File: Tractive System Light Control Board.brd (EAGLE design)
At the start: 88.2 x 39 mm, 70 parts, among them J1 MOLEX_CLICKMATE-2-VERTICAL, J2 MOLEX_CLICKMATE-2-VERTICAL, Q1 BSS138, T1 750313734, U1 ISO7221, U12 SN6501DBVR, U2 TPS562219, U21 LM1085IS, U3 SN74LVC1G04DRL, U36 LTC1155, U37 CSD17506Q5A, U38 LM124, U6 LTC1155, U8 CSD17506Q5A, U9 SN74LVC1G86DRL

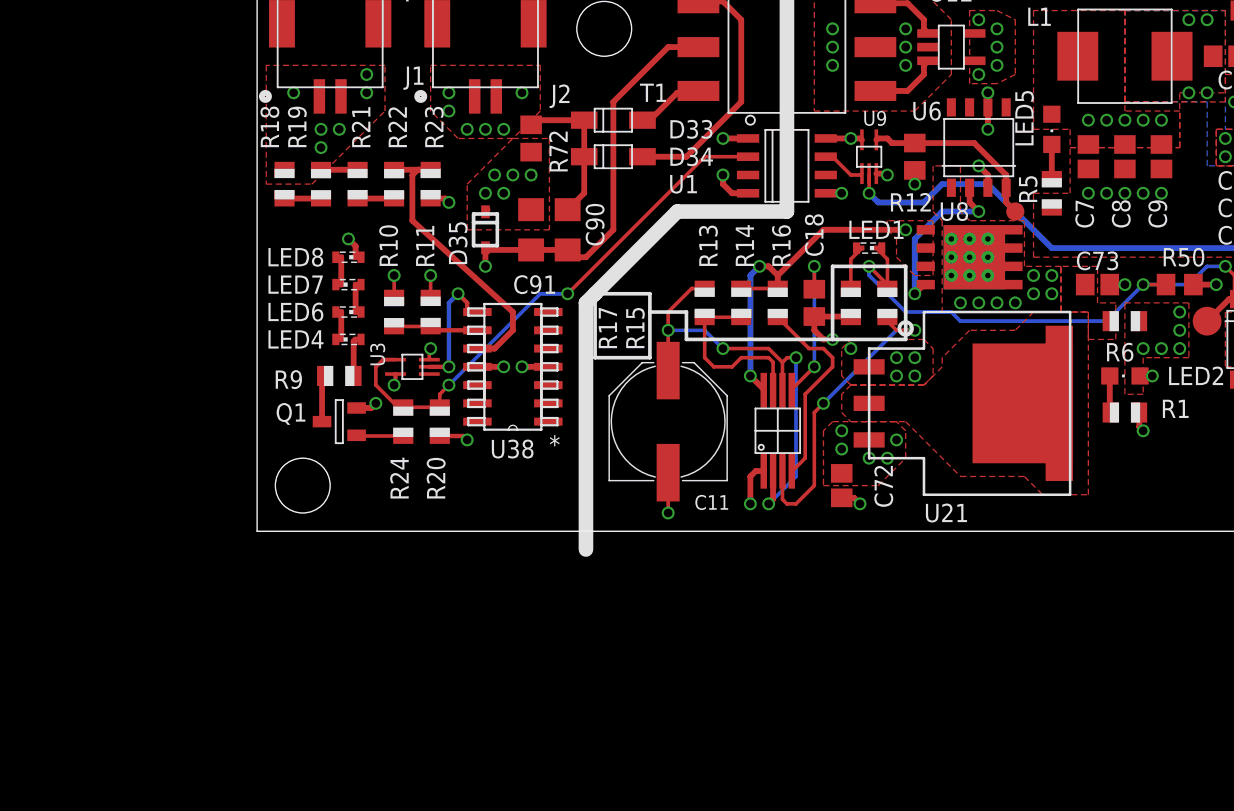
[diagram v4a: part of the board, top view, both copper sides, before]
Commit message: Reconfigured the schematic to improve functionality and readability
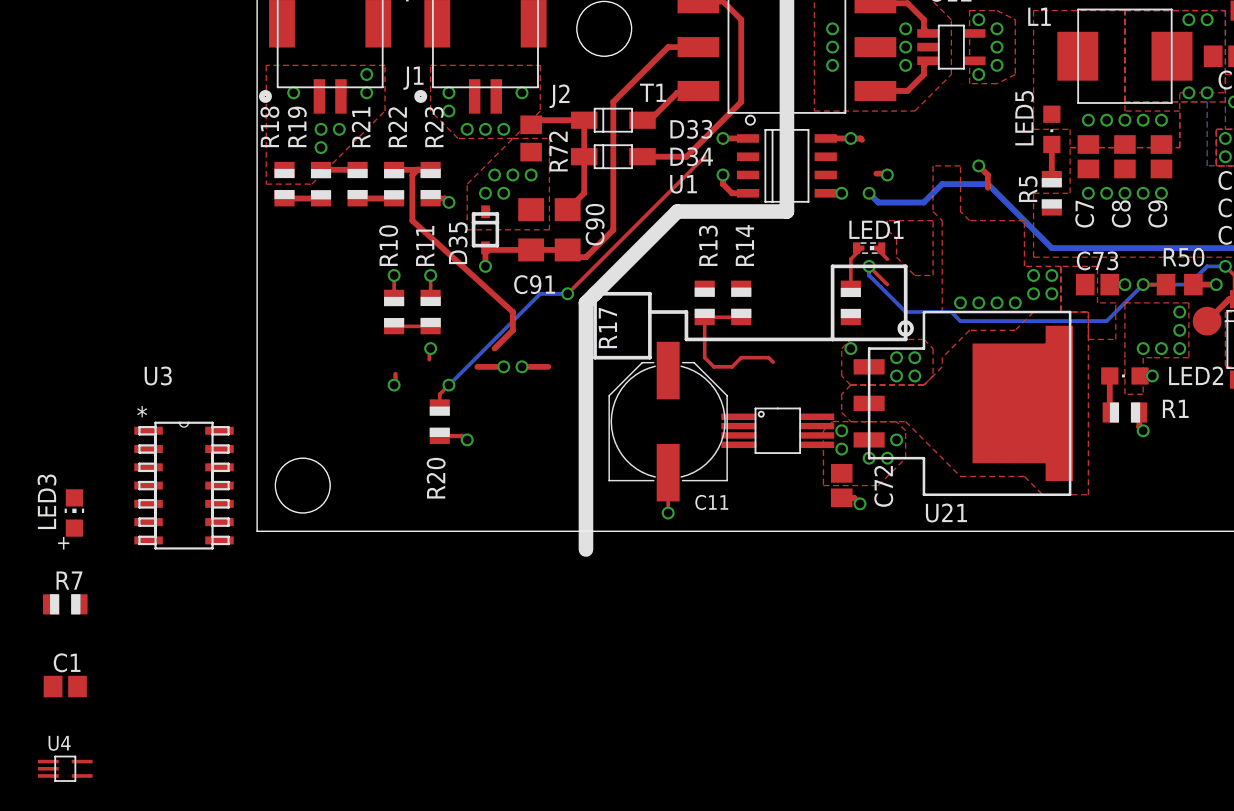
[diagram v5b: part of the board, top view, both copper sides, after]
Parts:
- removed C18: 100uF, rcl:C0805
- removed LED4, LED6, LED7, LED8: (no value), FormE:SMARTLED-TTW
- removed Q1: BSS138, FormE:BSS138
- removed R12: 10k, rcl:R0805
- removed R15: 0.33k, adafruit:R0805
- removed R16, R9: 1K, adafruit:R0805
- removed R24: 10, adafruit:R0805
- removed R6: 0.007, adafruit:R0805
- removed TP1: PTR1B1,27, testpad:B1,27
- removed U38: LM124, FormE:D14
- removed U6: LTC1155, FormE:LT-SOL8
- removed U8: CSD17506Q5A, FormE:SON_5X6
- removed U9: SN74LVC1G86DRL, FormE:LITTLE_LOGIC_BASIC_DRL
- added C1: 0.1uF, adafruit:C0805
- added LED3: (no value), FormE:CHIP-LED0805
- added R7: 10k, adafruit:R0805
- added U4: SN74LVC1G00DRL, FormE:LITTLE_LOGIC_BASIC_DRL
- J1, J2: value MOLEX_CLICKMATE-2-VERTICAL -> WM9811CT-ND
- R10: value 1.2k -> 10k
- R11: value 10k -> 47k
- R18: value 10k -> 140k
- R19, R21, R22: value 10k -> 120k
- T2: value (none) -> LMC555
- U3: value SN74LVC1G04DRL -> LM139; device FormE:LITTLE_LOGIC_BASIC_DRL -> FormE:D14
- moved U3 17.9 mm to (-5.08, 3.17), turned to 0 degrees
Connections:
- net LED_CONTROL_12V renamed TSAL_SUPPLY
- removed net 12V_CURRENT_SENSE+: C73.1, R6.1, U21.2, U21.GND, U21.GND1
- removed net 555_TIMER_SUPPLY: R14.1, R16.2, T2.P$1, U8.1, U8.2, U8.3
- removed net AMS_CONTACTOR_INVERTED: H1.4, U9.2
- removed net HV_INDICATOR_SIGNAL_LV: U1.P$7, U9.1
- removed net N$19: R16.1, T2.P$8
- removed net N$20: R15.1, T2.P$7
- removed net N$21: LED4.C@1, R9.2
- removed net N$22: LED4.A@1, LED6.C@1
- removed net N$24: LED6.A@1, LED7.C@1
- removed net N$25: LED7.A@1, LED8.C@1
- removed net N$35: U3.2, U38.8
- removed net N$49: Q1.G, R24.1
- removed net N$6: C11.+, R13.1, T2.P$3, T2.P$6
- removed net N$60: Q1.D, R9.1
- removed net N$8: U6.2, U8.4
- new net AIR_CLOSED: H1.4, U4.2
- new net N$4: U1.P$6, U4.1
- new net N$7: LED3.A, R7.2
- net +12V: now also C73.1, U21.2, U21.GND, U21.GND1; no longer R6.2
- net +5V: now also C1.1, R14.1, T2.8, U4.5; no longer U6.1, U6.6, U8.5, U8.6, U8.7, U8.8, U8.PAD, U8.PAD1, U8.VIA1, U8.VIA2, U8.VIA3, U8.VIA4, U8.VIA5, U8.VIA6, U8.VIA7, U8.VIA8, U8.VIA9, U9.5
- net +5V/1: now also R7.1, U3.3; no longer LED8.A@1, U3.5, U38.4
- net 555_TIMER_OUTPUT: now also T2.3; no longer R15.2
- net BATT_V_REFERENCE: now also U3.7; no longer U38.10
- net GND: now also C1.2, T2.1, U4.3; no longer C18.1, R12.1, T2.P$5, U6.3, U9.3
- net GND1: now also U3.12; no longer Q1.S, U3.3, U38.11
- net HV_INDICATOR_SIGNAL_HV: now also LED3.C, U1.P$3, U3.1; no longer R24.2, U1.P$2, U3.4
- net N$15: now also C11.+, R13.1, T2.2, T2.6; no longer C18.2, T2.P$4
- net N$48: now also U3.6; no longer U38.9
- net N$5: now also T2.7; no longer T2.P$2
- net N$9: now also T2.4, U4.4; no longer R12.2, TP1.TP, U6.4, U9.4
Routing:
- net AMS_CONTACTOR_INVERTED: track 47.4 -> 0.00 mm, vias 2 -> 0
- net AIR_CLOSED: track 0.00 -> 46.0 mm, vias 0 -> 2
- net N$6: track 32.5 -> 0.00 mm, vias 4 -> 0
- net 555_TIMER_SUPPLY: track 24.5 -> 0.00 mm, vias 3 -> 0
- net N$20: track 21.7 -> 0.00 mm, vias 2 -> 0
- net N$19: track 14.0 -> 0.00 mm
- net N$9: track 12.9 -> 0.00 mm
- net N$8: track 12.2 -> 0.00 mm, vias 2 -> 0
- net HV_INDICATOR_SIGNAL_HV: track 37.1 -> 26.2 mm
- net N$15: track 10.9 -> 0.00 mm, vias 2 -> 0
- net GND: track 28.7 -> 19.3 mm, vias 41 -> 38
- net N$35: track 8.95 -> 0.00 mm, vias 2 -> 0
- net N$60: track 3.64 -> 0.00 mm
- net N$49: track 3.27 -> 0.00 mm
- net HV_INDICATOR_SIGNAL_LV: track 3.08 -> 0.00 mm
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
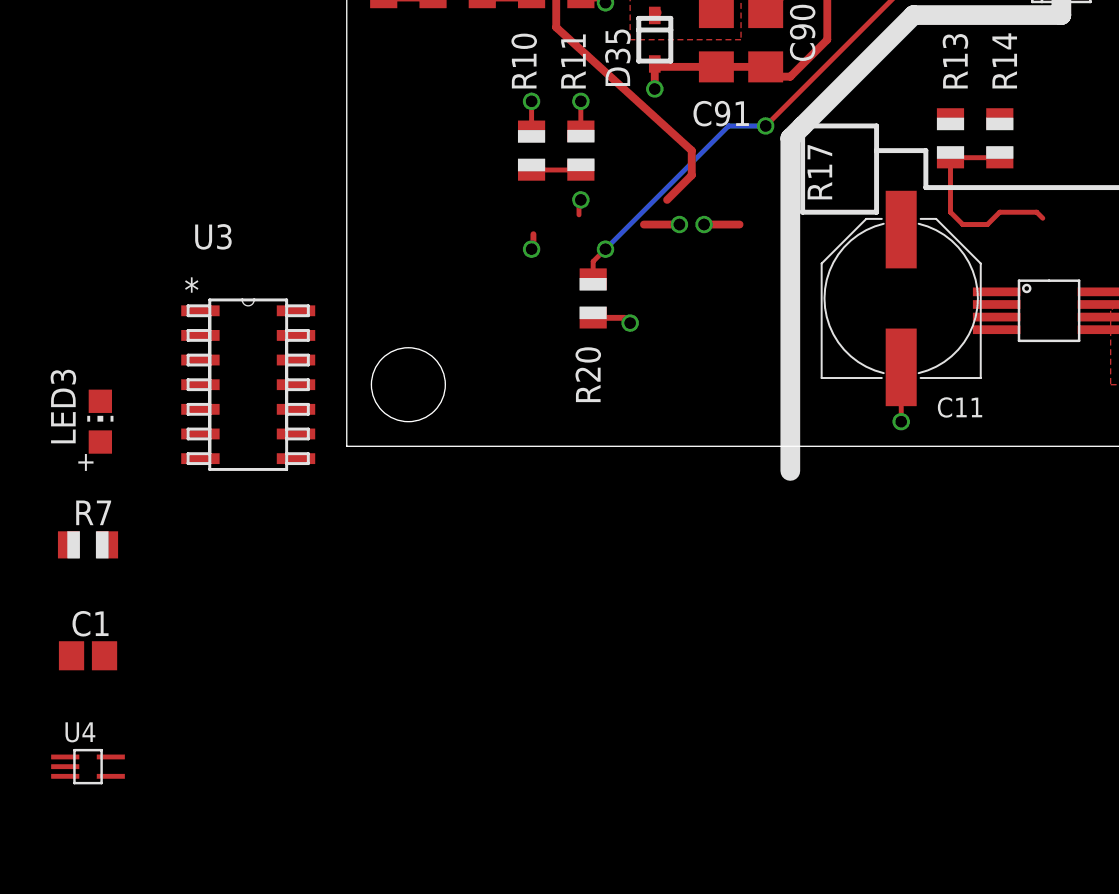
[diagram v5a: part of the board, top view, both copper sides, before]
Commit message: Changed RC values for 555 timer
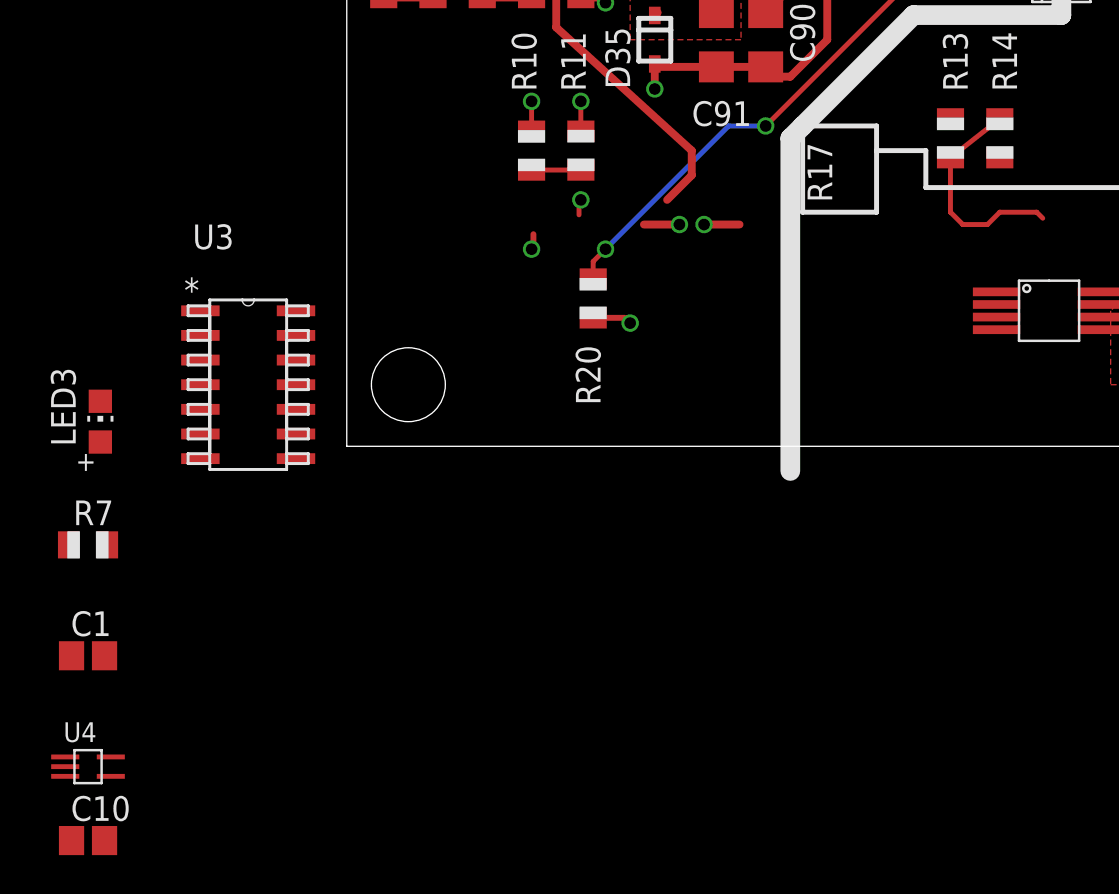
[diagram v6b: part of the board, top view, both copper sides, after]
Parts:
- removed C11: 100uF, adafruit:PANASONIC_F
- added C10: 10uF, adafruit:C0805
- LED3: value (none) -> RED
- R13: value 2k -> 20k
- R14: value 1.05k -> 10.5k
- R7: value 10k -> 1k
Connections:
- net +5V: now also R14.2; no longer R14.1
- net GND: now also C10.2; no longer C11.-
- net N$15: now also C10.1; no longer C11.+
- net N$5: now also R14.1; no longer R14.2
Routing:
- net GND: track 19.3 -> 16.5 mm, vias 38 -> 37
- net N$5: track 10.8 -> 11.5 mm
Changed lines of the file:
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@@
 </autorouter>
 <elements>
-<element name="C11" library="adafruit" package="PANASONIC_F" value="100uF" x="28.575" y="7.62" smashed="yes" rot="R90">
-<attribute name="PARTNO" value="EEE-1EA101XP" x="28.575" y="7.62" size="1.778" layer="27" rot="R90" display="off"/>
-<attribute name="NAME" x="32.865" y="2.51" size="1.016" layer="25" rot="R180"/>
-<attribute name="VALUE" x="30.95" y="5.87" size="1.016" layer="27" rot="R90"/>
-</element>
 <element name="J2" library="FormE" package="MOLEX-CLIKMATE-2-VERTICAL-HEADER" value="WM9811CT-ND" x="15.875" y="34.29" smashed="yes" rot="R180">
 <attribute name="NAME" x="21.875" y="31.036" size="1.27" layer="25" rot="R180"/>
@@
 <attribute name="VALUE" x="9.779" y="16.002" size="1.27" layer="27" rot="R270"/>
 </element>
-<element name="R13" library="adafruit" package="R0805" value="2k" x="31.115" y="15.875" smashed="yes" rot="R270">
+<element name="R13" library="adafruit" package="R0805" value="20k" x="31.115" y="15.875" smashed="yes" rot="R270">
 <attribute name="PARTNO" value="ERJ-6ENF2001V" x="31.115" y="15.875" size="1.778" layer="27" rot="R270" display="off"/>
 <attribute name="NAME" x="32.004" y="18.288" size="1.27" layer="25" rot="R90"/>
 <attribute name="VALUE" x="28.829" y="16.637" size="1.27" layer="27" rot="R270"/>
 </element>
-<element name="R14" library="adafruit" package="R0805" value="1.05k" x="33.655" y="15.875" smashed="yes" rot="R270">
+<element name="R14" library="adafruit" package="R0805" value="10.5k" x="33.655" y="15.875" smashed="yes" rot="R270">
 <attribute name="PARTNO" value="ERJ-6ENF1051V" x="33.655" y="15.875" size="1.778" layer="27" rot="R270" display="off"/>
 <attribute name="NAME" x="34.544" y="18.288" size="1.27" layer="25" rot="R90"/>
@@
 <attribute name="PIN_COUNT" value="14" x="-5.08" y="3.175" size="1.778" layer="27" display="off"/>
 </element>
-<element name="LED3" library="FormE" package="CHIP-LED0805" value="" x="-12.7" y="1.27"/>
-<element name="R7" library="adafruit" package="R0805" value="10k" x="-13.335" y="-5.08">
+<element name="LED3" library="FormE" package="CHIP-LED0805" value="RED" x="-12.7" y="1.27"/>
+<element name="R7" library="adafruit" package="R0805" value="1k" x="-13.335" y="-5.08">
 <attribute name="PARTNO" value="ERJ-6ENF1002V" x="-13.335" y="-5.08" size="1.778" layer="27" display="off"/>
 </element>
@@
 </element>
 <element name="U4" library="FormE" package="LITTLE_LOGIC_BASIC_DRL" value="SN74LVC1G00DRL" x="-13.335" y="-16.51"/>
+<element name="C10" library="adafruit" package="C0805" value="10uF" x="-13.335" y="-20.32">
+<attribute name="PARTNO" value="GRM21BR61E106KA73L" x="-13.335" y="-20.32" size="1.778" layer="27" display="off"/>
+</element>
 </elements>
 <signals>
@@
 <contactref element="R17" pad="1"/>
 <contactref element="U36" pad="3"/>
-<contactref element="C11" pad="-"/>
-<wire x1="28.575" y1="4.07" x2="28.575" y2="1.27" width="0.254" layer="1"/>
-<via x="28.575" y="1.27" extent="1-16" drill="0.6"/>
 <wire x1="41.225" y1="14.925" x2="41.275" y2="14.875" width="0.4064" layer="1"/>
 <polygon width="0.254" layer="1" rank="2">
@@
 <contactref element="C1" pad="2"/>
 <contactref element="U4" pad="3"/>
+<contactref element="C10" pad="2"/>
 <wire x1="69.85" y1="34.29" x2="76.415" y2="34.505" width="0" layer="19" extent="1-1"/>
 <wire x1="69.215" y1="31.115" x2="69.85" y2="34.29" width="0" layer="19" extent="1-1"/>
@@
 <wire x1="41.49" y1="2.325" x2="44.45" y2="10.795" width="0" layer="19" extent="1-1"/>
 <wire x1="33.495" y1="7.96" x2="41.275" y2="12.7" width="0" layer="19" extent="1-1"/>
-<wire x1="28.575" y1="4.07" x2="33.495" y2="7.96" width="0" layer="19" extent="1-1"/>
-<wire x1="-12.485" y1="-10.795" x2="28.575" y2="1.27" width="0" layer="19" extent="1-1"/>
+<wire x1="-12.485" y1="-10.795" x2="33.495" y2="7.96" width="0" layer="19" extent="1-1"/>
 <wire x1="-14.51" y1="-17.01" x2="-12.485" y2="-10.795" width="0" layer="19" extent="1-1"/>
+<wire x1="-12.485" y1="-20.32" x2="-14.51" y2="-17.01" width="0" layer="19" extent="1-1"/>
 </signal>
 <signal name="VCC">
@@
 <wire x1="41.95" y1="27.305" x2="42.045" y2="27.21" width="0.4064" layer="1"/>
 <wire x1="39.53" y1="27.305" x2="41.275" y2="27.305" width="0.4064" layer="1"/>
-<contactref element="R14" pad="1"/>
+<contactref element="R14" pad="2"/>
 <contactref element="C1" pad="1"/>
 <contactref element="T2" pad="8"/>
@@
 <wire x1="39.53" y1="27.305" x2="40.005" y2="32.385" width="0" layer="19" extent="1-1"/>
 <wire x1="65.085" y1="17.145" x2="55.245" y2="17.78" width="0" layer="19" extent="1-1"/>
-<wire x1="33.655" y1="16.875" x2="39.53" y2="27.305" width="0" layer="19" extent="1-1"/>
-<wire x1="38.895" y1="7.96" x2="33.655" y2="16.875" width="0" layer="19" extent="1-1"/>
-<wire x1="-14.185" y1="-10.795" x2="33.655" y2="16.875" width="0" layer="19" extent="1-1"/>
+<wire x1="33.655" y1="14.875" x2="39.53" y2="27.305" width="0" layer="19" extent="1-1"/>
+<wire x1="38.895" y1="7.96" x2="33.655" y2="14.875" width="0" layer="19" extent="1-1"/>
+<wire x1="-14.185" y1="-10.795" x2="33.655" y2="14.875" width="0" layer="19" extent="1-1"/>
 <wire x1="-12.16" y1="-16.01" x2="-14.185" y2="-10.795" width="0" layer="19" extent="1-1"/>
 </signal>
@@
 </signal>
 <signal name="N$5">
-<contactref element="R14" pad="2"/>
+<contactref element="R14" pad="1"/>
 <contactref element="R13" pad="2"/>
 <wire x1="35.56" y1="12.065" x2="33.655" y2="12.065" width="0.254" layer="1"/>
@@
 <wire x1="31.75" y1="11.43" x2="31.115" y2="12.065" width="0.254" layer="1"/>
 <wire x1="31.115" y1="12.065" x2="31.115" y2="14.875" width="0.254" layer="1"/>
-<wire x1="31.115" y1="14.875" x2="33.655" y2="14.875" width="0.254" layer="1"/>
+<wire x1="31.115" y1="14.875" x2="33.655" y2="16.875" width="0.254" layer="1"/>
 <wire x1="35.87" y1="11.755" x2="35.56" y2="12.065" width="0.254" layer="1"/>
 <contactref element="T2" pad="7"/>
@@
 <contactref element="T2" pad="6"/>
 <contactref element="R13" pad="1"/>
-<contactref element="C11" pad="+"/>
-<wire x1="28.575" y1="11.17" x2="31.115" y2="16.875" width="0" layer="19" extent="1-1"/>
-<wire x1="38.895" y1="6.66" x2="28.575" y2="11.17" width="0" layer="19" extent="1-1"/>
-<wire x1="33.495" y1="7.31" x2="38.895" y2="6.66" width="0" layer="19" extent="1-1"/>
+<contactref element="C10" pad="1"/>
+<wire x1="33.495" y1="7.31" x2="31.115" y2="16.875" width="0" layer="19" extent="1-1"/>
+<wire x1="38.895" y1="6.66" x2="33.495" y2="7.31" width="0" layer="19" extent="1-1"/>
+<wire x1="-14.185" y1="-20.32" x2="33.495" y2="7.31" width="0" layer="19" extent="1-1"/>
 </signal>
 </signals>
